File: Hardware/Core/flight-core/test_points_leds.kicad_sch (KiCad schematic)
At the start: 22 parts

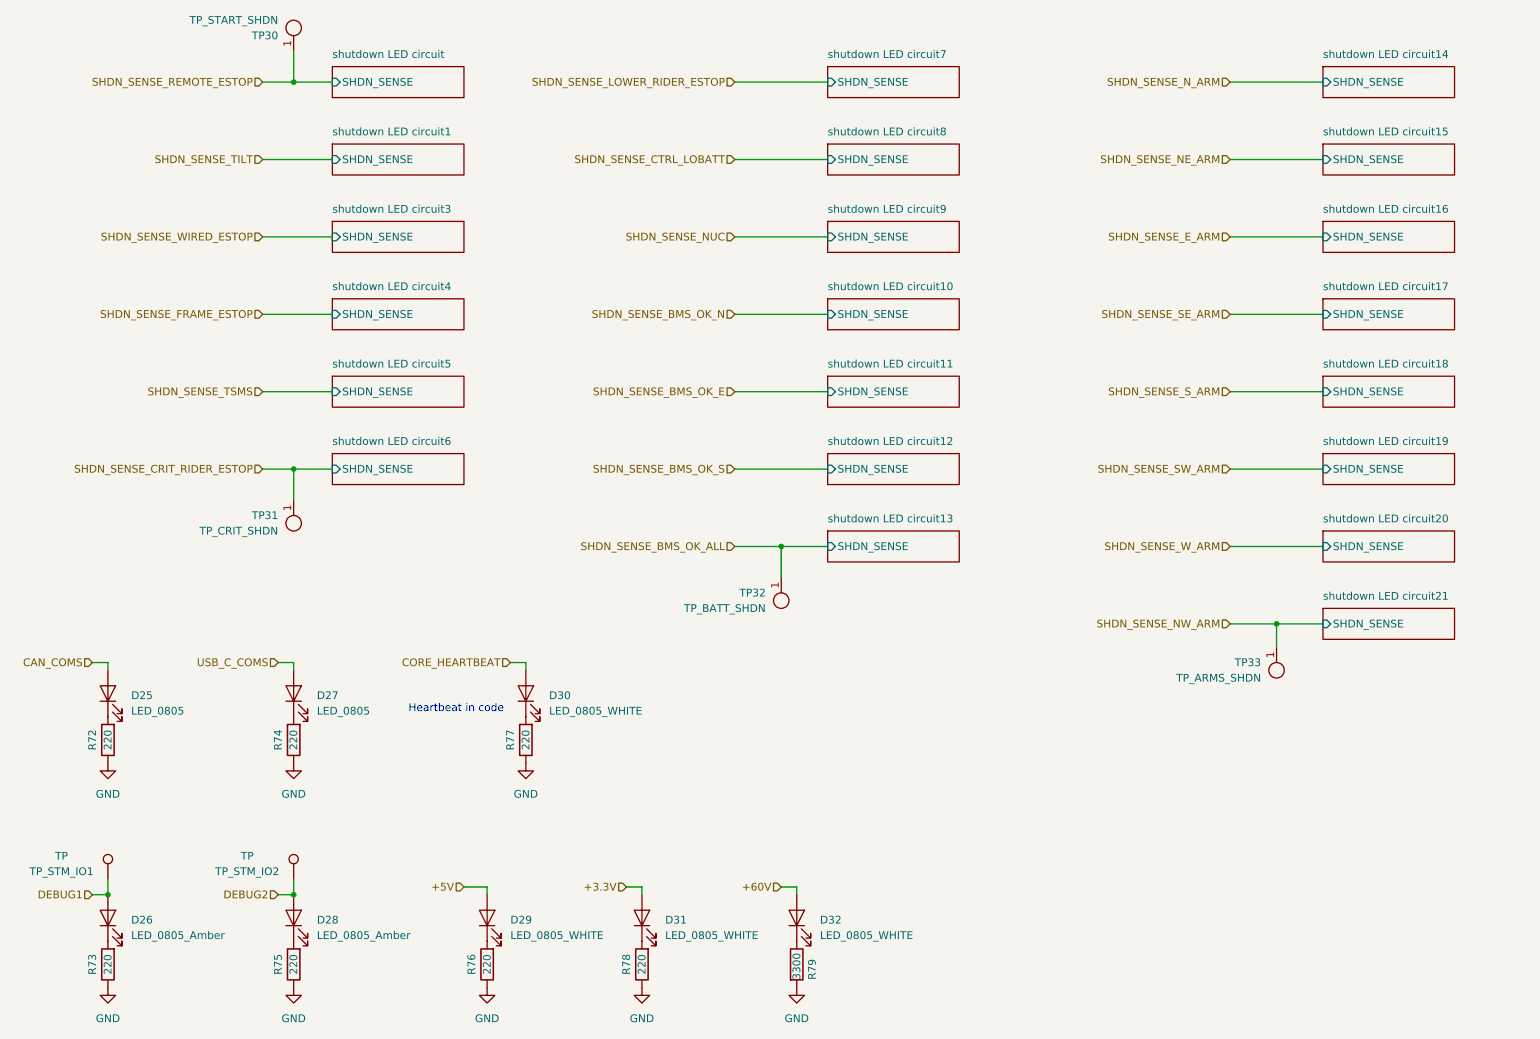
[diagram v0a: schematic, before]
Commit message: removed extra test points, removed debug2, reannotated schem
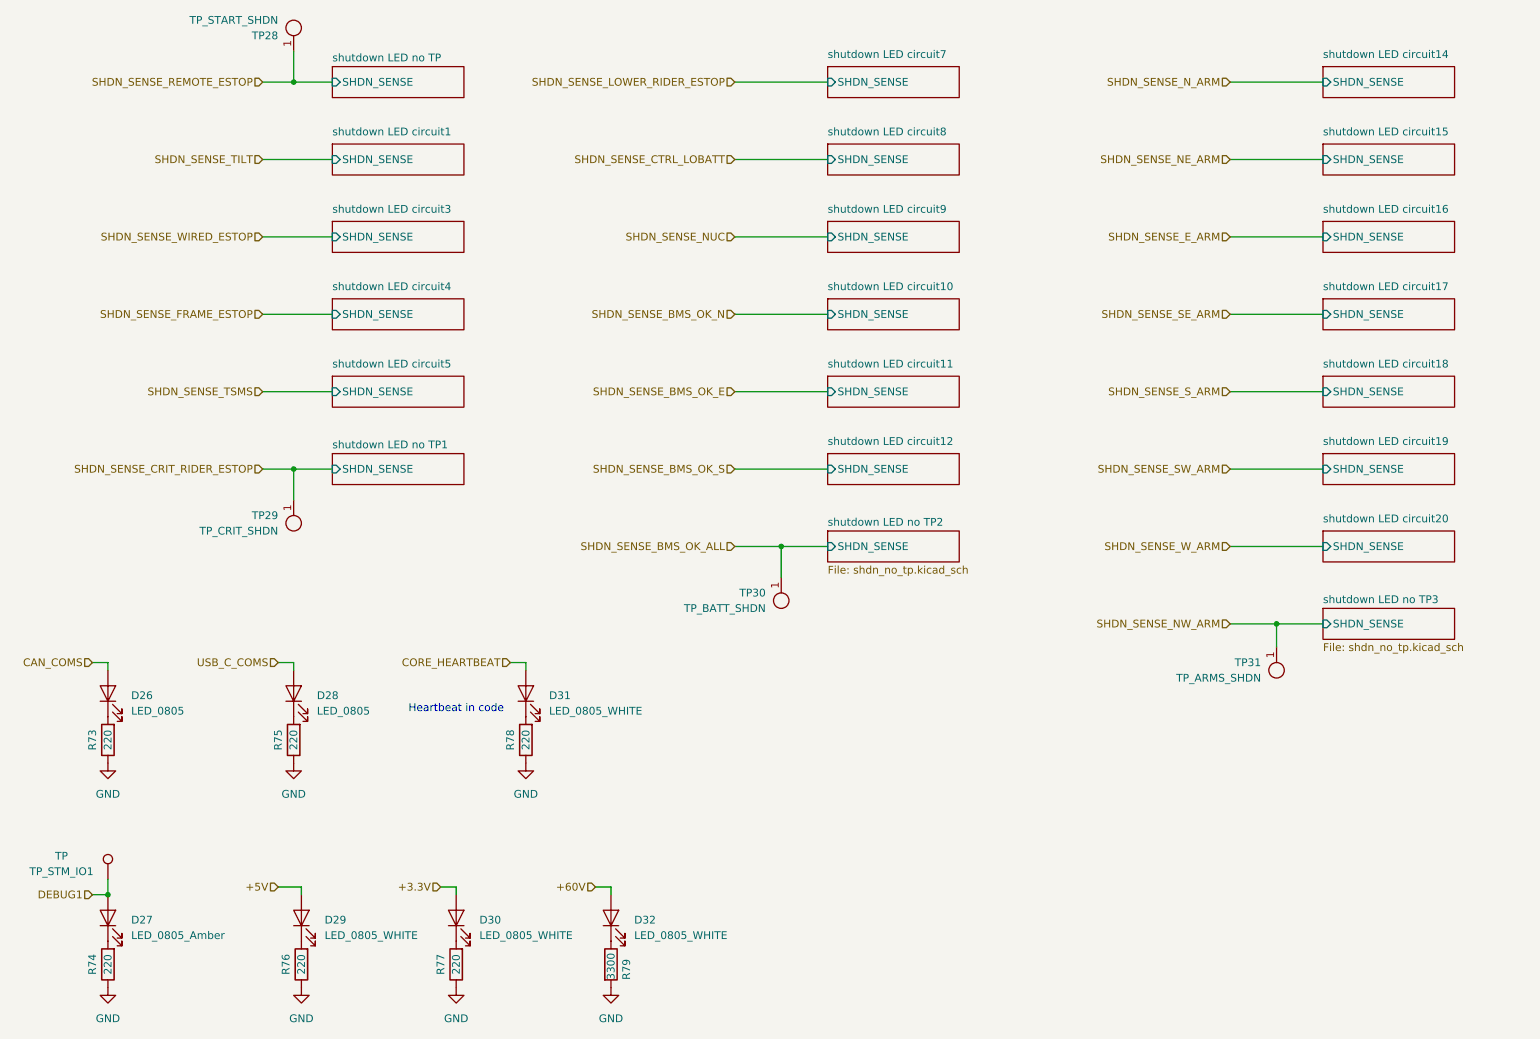
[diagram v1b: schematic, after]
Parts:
- removed D28: LED_0805_Amber, footprints:LED_0805_OEM, symbol formula:LED_0805_Amber
- removed R75: 220, footprints:R_0603_1608Metric, symbol Device:R
- removed TP_STM_IO2: TP, obad_footprints:TestPoint_Pad_D1.0mm, symbol OlinBAD:D1.0_TP
- renumbered D25 to D26, D26 to D27, D27 to D28, D31 to D30, D30 to D31, R72 to R73, R73 to R74, R74 to R75, R78 to R77, R77 to R78, TP30 to TP28, TP31 to TP29, TP32 to TP30, TP33 to TP31
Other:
- removed sheet shutdown LED circuit
- removed sheet shutdown LED circuit13
- removed sheet shutdown LED circuit21
- removed sheet shutdown LED circuit6
- added sheet shutdown LED no TP (shdn_no_tp.kicad_sch)
- added sheet shutdown LED no TP1 (shdn_no_tp.kicad_sch)
- added sheet shutdown LED no TP2 (shdn_no_tp.kicad_sch)
- added sheet shutdown LED no TP3 (shdn_no_tp.kicad_sch)
- moved on the sheet: D29, D30, D32, R76, R77, R79

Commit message: Major reroute & semi-final update
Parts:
- removed D32: LED_0805_WHITE, footprints:LED_0805_OEM, symbol OlinBAD:LED_0805_WHITE
- removed R79: 3300, footprints:R_0603_1608Metric, symbol Device:R
- removed TP30: TP_BATT_SHDN, footprints:Test_Point_SMD, symbol formula:TP_SMD
- added D3601: LED_0805_Blue, footprints:LED_0805_OEM, symbol formula:LED_0805_Amber
- added D3602, D3603: LED_0805_Amber, footprints:LED_0805_OEM, symbol formula:LED_0805_Amber
- added Q3601: MMBF170, Package_TO_SOT_SMD:SOT-23, symbol formula:MMBF170
- added R3601, R3602, R3603: 200, footprints:R_0603_1608Metric, symbol formula:R_200
- added TP3701: TP_ARMS_SHDN, TestPoint:TestPoint_Keystone_5019_Miniature, symbol formula:TP_SMD
- TP28, TP29, TP31: footprint footprints:Test_Point_SMD -> TestPoint:TestPoint_Keystone_5019_Miniature
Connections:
- net +5V: now also D3601.2 (A), D3602.2 (A), D3603.2 (A)
- net GND: now also Q3601.2 (S)
- net SHDN_SENSE_BMS_OK_ALL: now also TP3701.1
- net SHDN_SENSE_NW_ARM: now also Q3601.1 (G)
- new net: D3601.1 (K), R3601.1
- new net: Q3601.3 (D), R3601.2, R3602.2, R3603.2
- new net: D3602.1 (K), R3602.1
- new net: D3603.1 (K), R3603.1
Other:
- removed sheet shutdown LED no TP3
- moved on the sheet: TP31
